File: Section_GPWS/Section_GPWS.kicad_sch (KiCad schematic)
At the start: 24 parts, among them J1 APU ribbon, J2 Backlight, SW1 APU MASTER SW, SW2 APU START

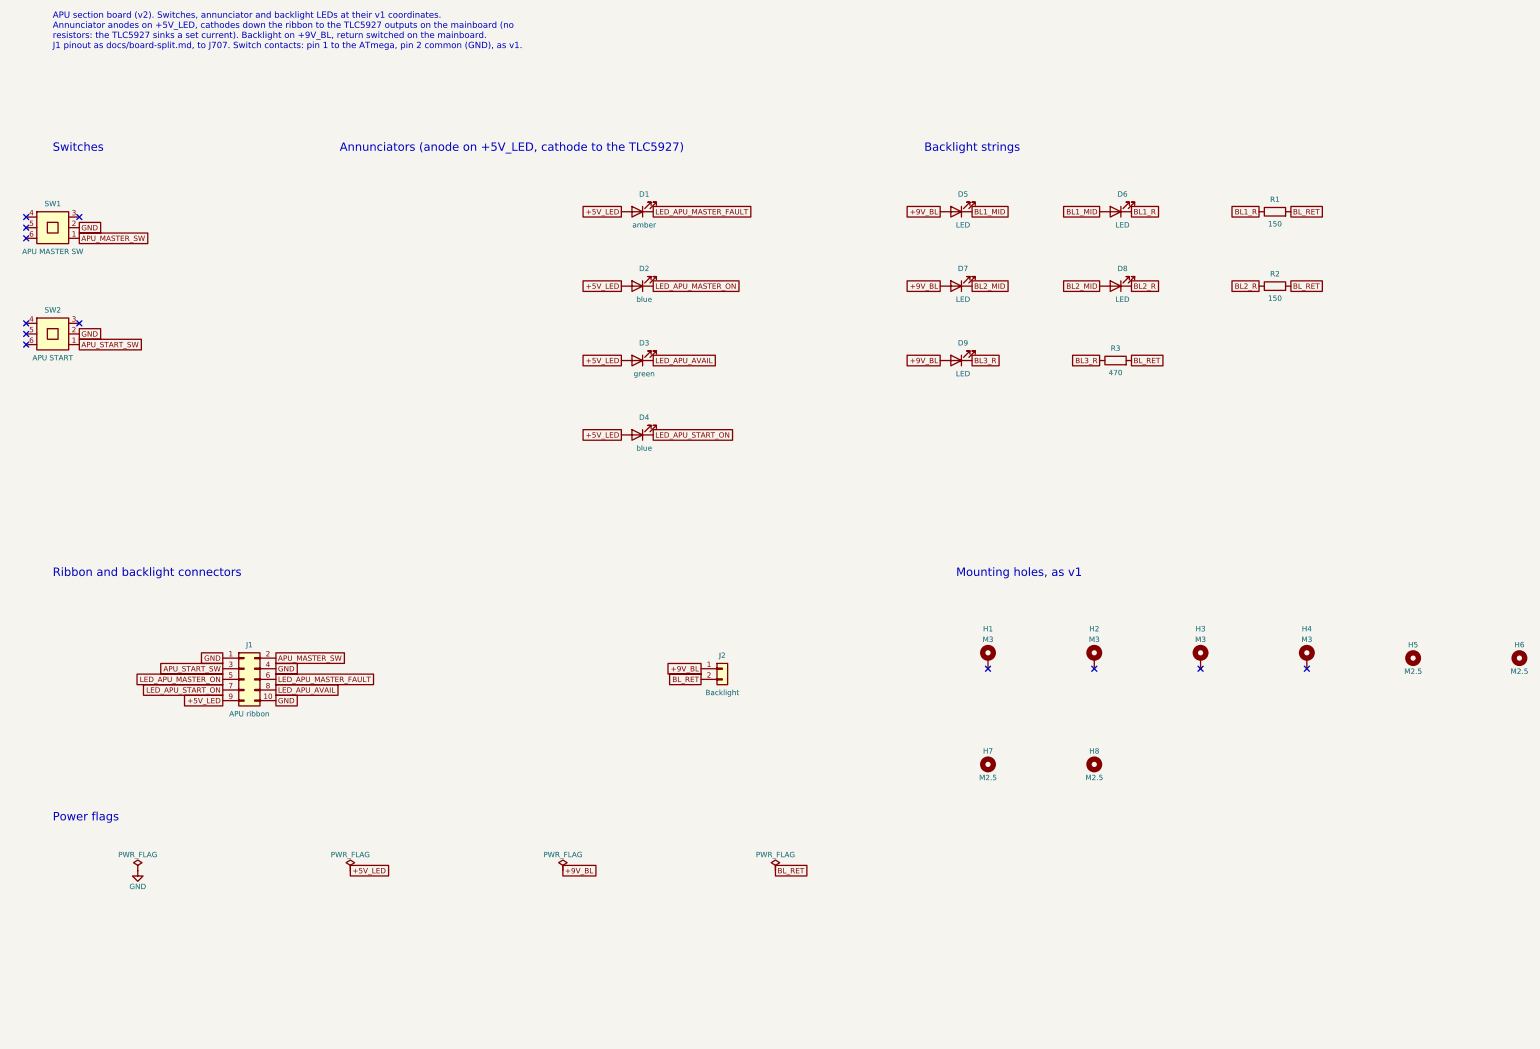
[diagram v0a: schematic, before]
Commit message: Add the GPWS section board, from a builder shared by all section boards
One builder now makes every section board from a short description (v1
parts, backlight strings, new part positions) and checks it against the v1
copper, not net names: each switch contact must reach its ATmega pin, each
annunciator cathode its TLC5927 output, each backlight string must be
chained as described. APU rebuilt with it: same nets and values, only the
part descriptions reworded.

GPWS: 4 Korry, 6 annunciators, 4 strings of two and D139 on its own with a
new 470 ohm (D140 and R75, its v1 partners, belong to EXT LT). J1 2x7 and
J2 on the back along the top edge. ERC 0, DRC 0, nothing unconnected, no
schematic-parity issues.

Co-Authored-By: Claude Opus 5.5 <noreply@anthropic.com>
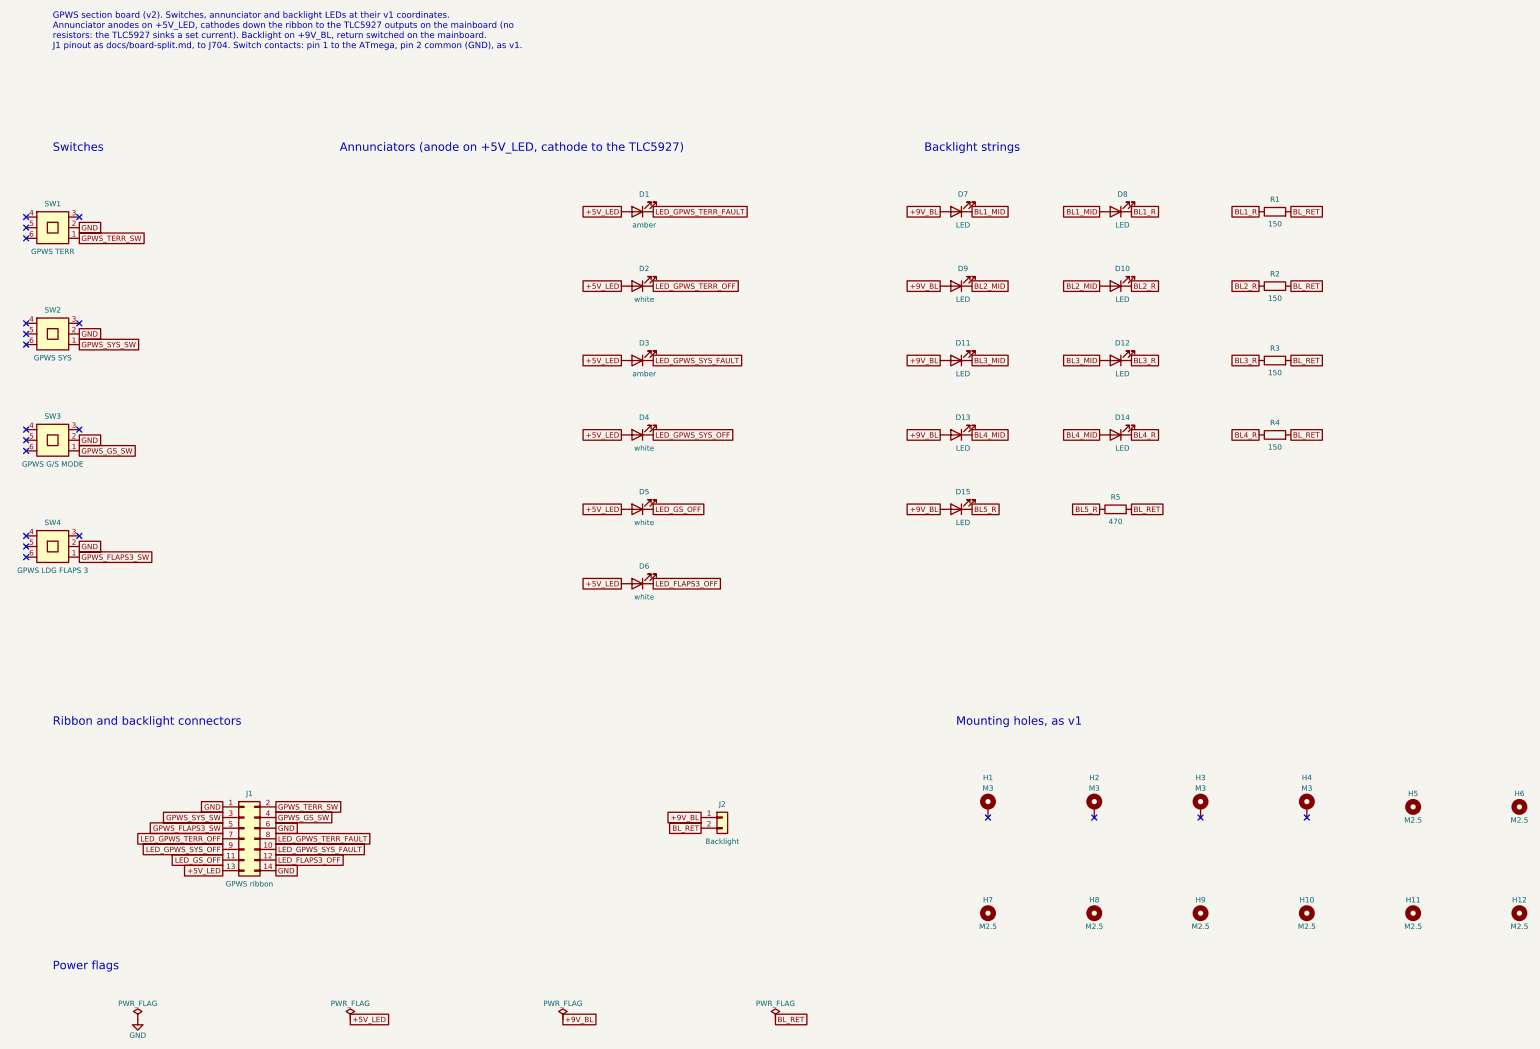
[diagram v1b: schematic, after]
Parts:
- removed J1: APU ribbon, Connector_IDC:IDC-Header_2x05_P2.54mm_Vertical_SMD, symbol Connector_Generic:Conn_02x05_Odd_Even
- added D10, D11, D12, D13, D14, D15: LED, LED_SMD:LED_1206_3216Metric_Pad1.42x1.75mm_HandSolder, symbol Device:LED
- added H10, H11, H12, H9: M2.5, MountingHole:MountingHole_2.7mm_M2.5, symbol Mechanical:MountingHole
- added J1: GPWS ribbon, Connector_IDC:IDC-Header_2x07_P2.54mm_Vertical_SMD, symbol Connector_Generic:Conn_02x07_Odd_Even
- added R4: 150, Resistor_SMD:R_1206_3216Metric_Pad1.30x1.75mm_HandSolder, symbol Device:R
- added R5: 470, Resistor_SMD:R_1206_3216Metric_Pad1.30x1.75mm_HandSolder, symbol Device:R
- added SW3: GPWS G/S MODE, OVHD:G-Switch_PS-7054DVB-6PN, symbol OVHD:Korry_PS-7054DVB-6PN
- added SW4: GPWS LDG FLAPS 3, OVHD:G-Switch_PS-7054DVB-6PN, symbol OVHD:Korry_PS-7054DVB-6PN
- D2, D4: value blue -> white
- D3: value green -> amber
- D5, D6: value LED -> white; footprint LED_SMD:LED_1206_3216Metric_Pad1.42x1.75mm_HandSolder -> OVHD:LED_Rectangular_W3.9mm_H1.8mm_FlatTop
- R3: value 470 -> 150
- SW1: value APU MASTER SW -> GPWS TERR
- SW2: value APU START -> GPWS SYS
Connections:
- net +5V_LED: now also D5.2 (A), D6.2 (A), J1.13 (Pin_13)
- net +9V_BL: now also D11.2 (A), D13.2 (A), D15.2 (A); no longer D5.2 (A)
- net BL1_MID: now also D7.1 (K), D8.2 (A); no longer D5.1 (K), D6.2 (A)
- net BL1_R: now also D8.1 (K); no longer D6.1 (K)
- net BL2_MID: now also D9.1 (K), D10.2 (A); no longer D7.1 (K), D8.2 (A)
- net BL2_R: now also D10.1 (K); no longer D8.1 (K)
- net BL3_R: now also D12.1 (K); no longer D9.1 (K)
- net BL_RET: now also R4.2, R5.2
- net GND: now also J1.1 (Pin_1), J1.14 (Pin_14), J1.6 (Pin_6), SW3.2, SW4.2
- net APU_MASTER_SW renamed GPWS_TERR_SW
- net GPWS_TERR_SW: now also J1.2 (Pin_2)
- net APU_START_SW renamed GPWS_SYS_SW
- net GPWS_SYS_SW: now also J1.3 (Pin_3)
- net LED_APU_AVAIL renamed LED_GPWS_SYS_FAULT
- net LED_GPWS_SYS_FAULT: now also J1.10 (Pin_10)
- net LED_APU_MASTER_FAULT renamed LED_GPWS_TERR_FAULT
- net LED_GPWS_TERR_FAULT: now also J1.8 (Pin_8)
- net LED_APU_MASTER_ON renamed LED_GPWS_TERR_OFF
- net LED_GPWS_TERR_OFF: now also J1.7 (Pin_7)
- net LED_APU_START_ON renamed LED_GPWS_SYS_OFF
- net LED_GPWS_SYS_OFF: now also J1.9 (Pin_9)
- new net BL3_MID: D11.1 (K), D12.2 (A)
- new net BL4_MID: D13.1 (K), D14.2 (A)
- new net BL4_R: D14.1 (K), R4.1
- new net BL5_R: D15.1 (K), R5.1
- new net GPWS_FLAPS3_SW: J1.5 (Pin_5), SW4.1
- new net GPWS_GS_SW: J1.4 (Pin_4), SW3.1
- new net LED_FLAPS3_OFF: D6.1 (K), J1.12 (Pin_12)
- new net LED_GS_OFF: D5.1 (K), J1.11 (Pin_11)
- no-connect marks 12 -> 20
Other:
- note added: "GPWS section board (v2). Switches, annunciator and backlight LEDs at their v1 coordinates. Annunciator anodes on +5V_LED, cathodes down the ribbon to the TLC5927 outputs on the mainboard (no resistors: the TLC5927 sinks a set current). Backlight on +9V_BL, return switched on the mainboard. J1 pinout as docs/board-split.md, to J704. Switch contacts: pin 1 to the ATmega, pin 2 common (GND), as v1."
- note removed: "APU section board (v2). Switches, annunciator and backlight LEDs at their v1 coordinates. Annunciator anodes on +5V_LED, cathodes down the ribbon to the TLC5927 outputs on the mainboard (no resistors: the TLC5927 sinks a set current). Backlight on +9V_BL, return switched on the mainboard. J1 pinout as docs/board-split.md, to J707. Switch contacts: pin 1 to the ATmega, pin 2 common (GND), as v1."
- title: APU section board -> GPWS section board

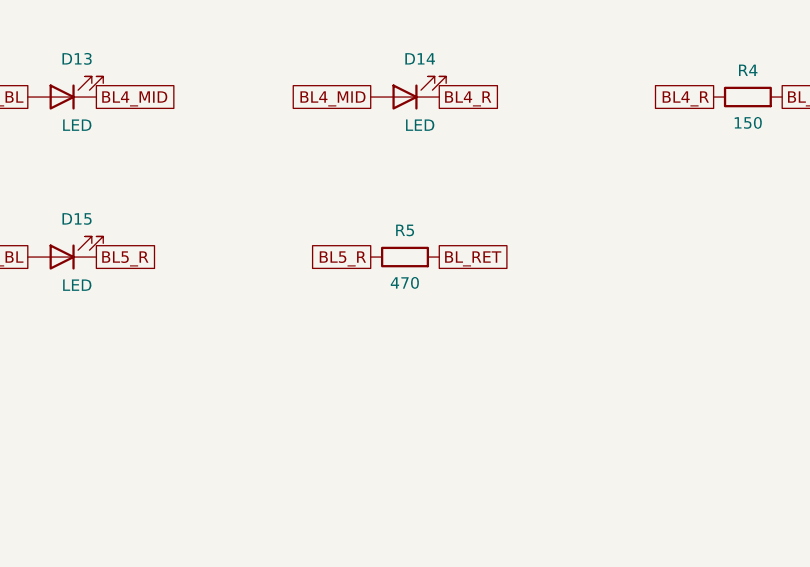
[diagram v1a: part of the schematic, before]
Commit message: Single-LED backlight strings on 330 ohm, not 470
A pair of backlight LEDs on 150 ohm runs at 17 mA (Stefano's figure). The
470 ohm came from an estimated 11 mA per string, which was wrong. For the
same 17 mA a single LED needs V / (2 I) + 75 ohm = 330 ohm. Changed on APU
(R3), GPWS (R5), AIR COND (R7, the v1 R76) and EXT LT (R16); the document's
backlight currents now use 17 mA, ~1.1 A in all. The four boards rebuilt
and rerouted: ERC 0, DRC 0, nothing unconnected, no parity issues.

Co-Authored-By: Claude Opus 5.5 <noreply@anthropic.com>
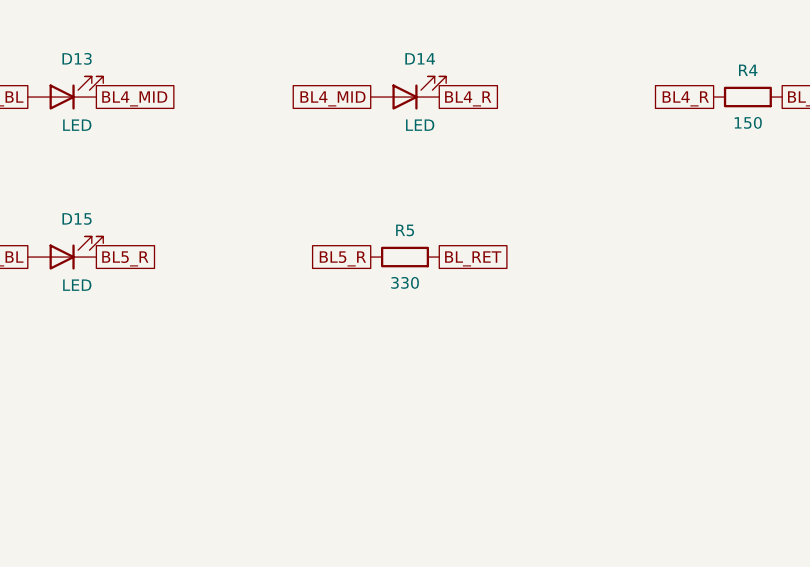
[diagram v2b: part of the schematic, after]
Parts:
- R5: value 470 -> 330
